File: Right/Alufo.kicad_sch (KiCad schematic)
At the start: 42 parts, among them J1 USB_C_Receptacle_USB2.0_16P_2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, J2 USB_C_Receptacle_USB2.0_16P_2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, J3 USB_C_Receptacle_USB2.0_16P_2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, J4 USB_C_Receptacle_USB2.0_16P_2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, SW10 BOOT, U1 CH552T, U2 CH552T, U3 USBLC6-2P6, U4 USBLC6-2P6, U5 USBLC6-2P6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

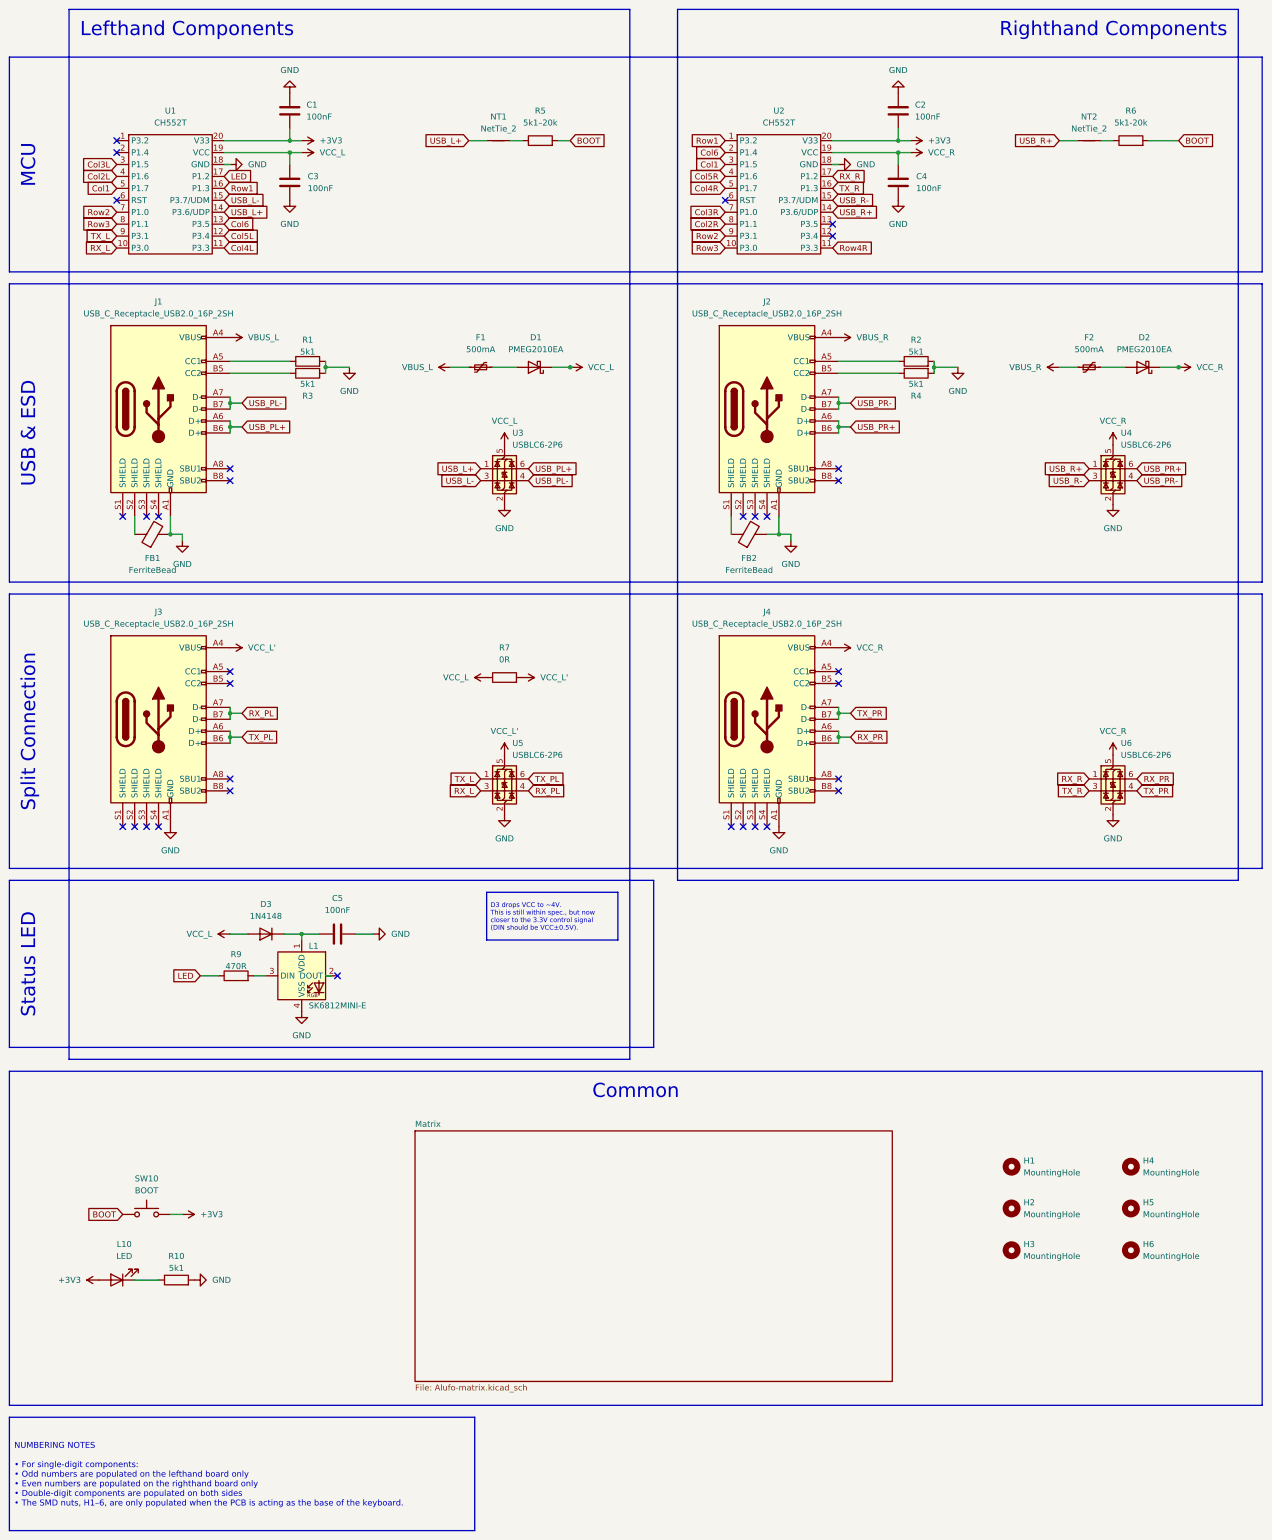
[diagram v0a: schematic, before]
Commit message: Remove lefthand components from righthand board
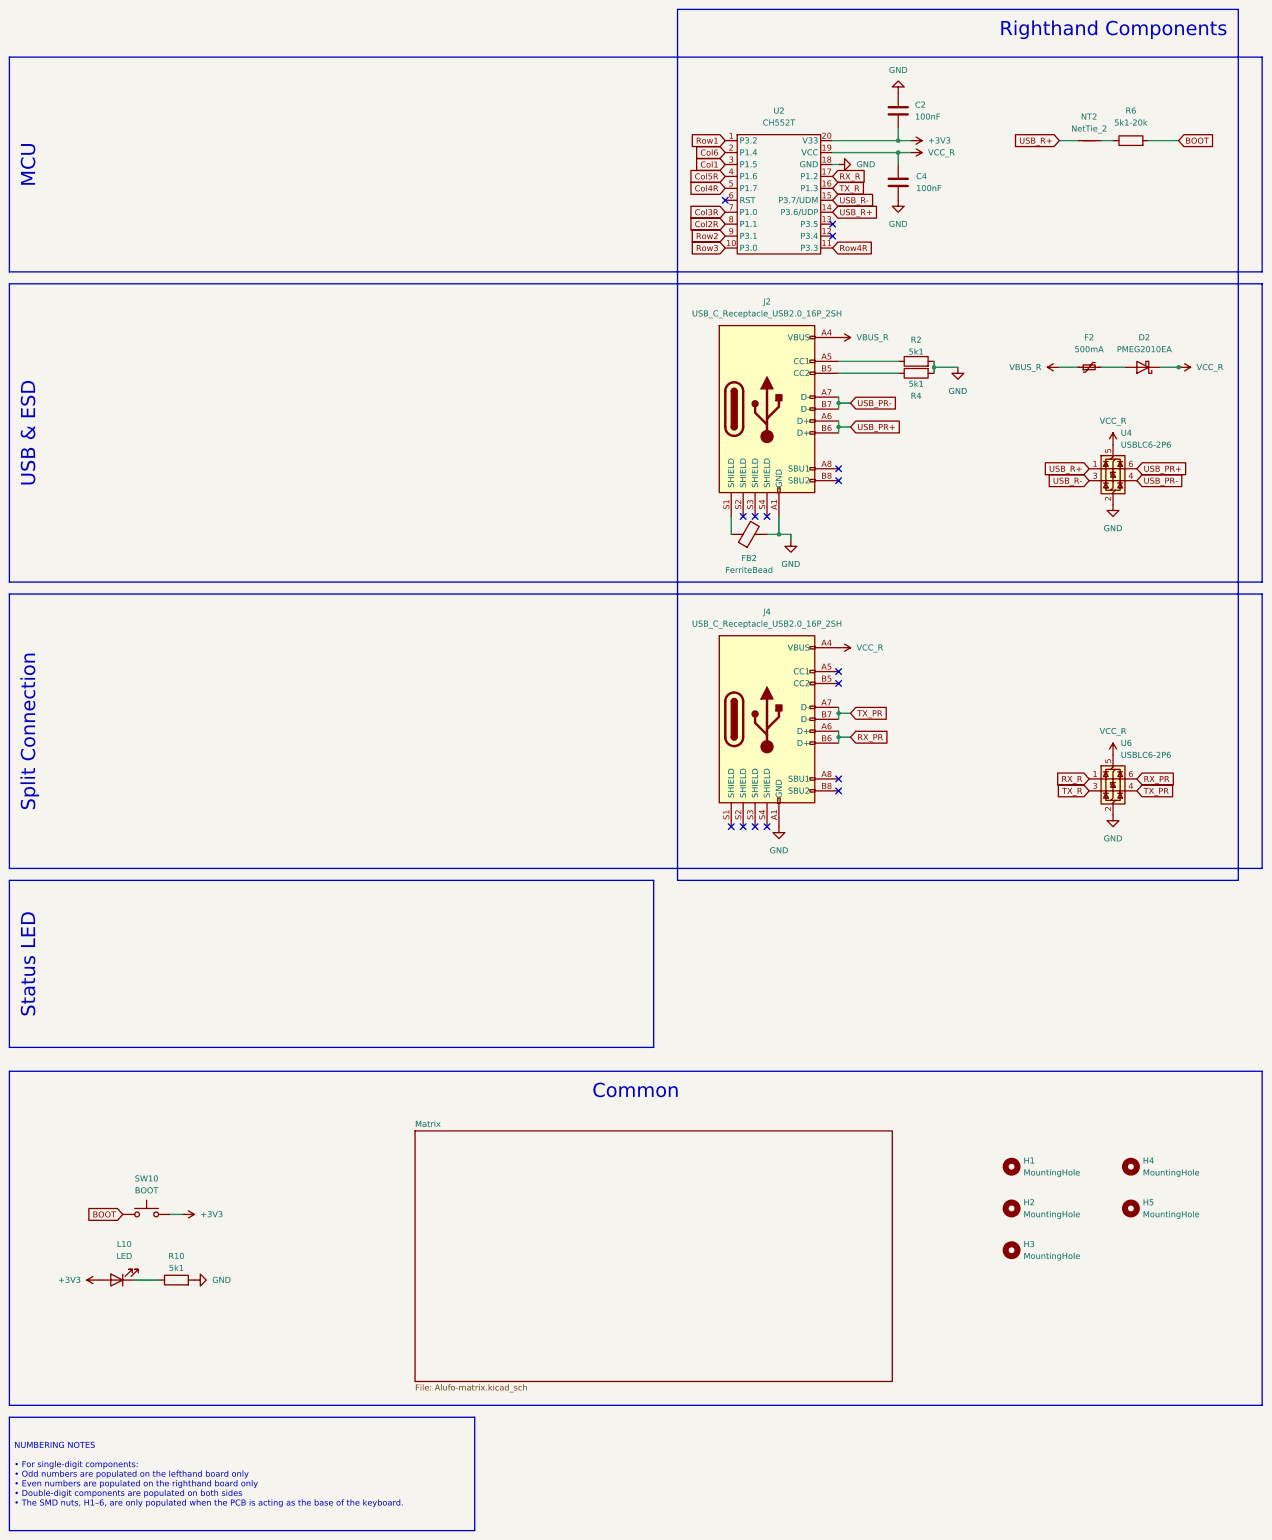
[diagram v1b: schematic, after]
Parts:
- removed C1, C3, C5: 100nF, Capacitor_SMD:C_0603_1608Metric, symbol Device:C
- removed D1: PMEG2010EA, Diode_SMD:D_SOD-323, symbol Device:D_Schottky
- removed D3: 1N4148, Project Library:D_SOD-123, symbol Device:D
- removed F1: 500mA, Fuse:Fuse_0603_1608Metric, symbol Device:Polyfuse_Small
- removed FB1: FerriteBead, Inductor_SMD:L_0805_2012Metric, symbol Device:FerriteBead
- removed H6: MountingHole, Project Library:MountingHole_2.2mm_M2_SMD_Solder_Nut, symbol Mechanical:MountingHole
- removed J1, J3: USB_C_Receptacle_USB2.0_16P_2SH, Project Library:USB_C_Receptacle_HRO_TYPE-C-31-M-12, symbol Project Library:USB_C_Receptacle_USB2.0_16P_2SH
- removed L1: SK6812MINI-E, PCM_marbastlib-various:LED_6028R, symbol PCM_marbastlib-various:SK6812MINI-E
- removed NT1: NetTie_2, Project Library:NetTie-2_SMD_Pad0.2mm, symbol Device:NetTie_2
- removed R1, R3: 5k1, Resistor_SMD:R_0603_1608Metric, symbol Device:R
- removed R5: 5k1–20k, Resistor_SMD:R_0603_1608Metric, symbol Device:R
- removed R7: 0R, Resistor_SMD:R_2010_5025Metric, symbol Device:R
- removed R9: 470R, Resistor_SMD:R_0805_2012Metric, symbol Device:R
- removed U1: CH552T, Package_SO:TSSOP-20_4.4x6.5mm_P0.65mm, symbol Project Library:MCU_CH552T_TSSOP-20
- removed U3, U5: USBLC6-2P6, Project Library:SOT-666_Mod, symbol Power_Protection:USBLC6-2P6
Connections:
- no-connect marks 33 -> 16
